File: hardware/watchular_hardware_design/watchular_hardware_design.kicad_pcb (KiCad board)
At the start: 4 copper layers, 55.5 x 22.9 mm, 90 parts, among them J1 USB4105-GF-A, J2 665102131822, J3 TSW-116-07-H-S, J4 TSW-116-07-H-S, Q1 BSS123, Q2 BSS123, Q3 BSS123, Q4 BSS123, T1 DMG1013UW-7, U1 MCP73832T-2DCI/OT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

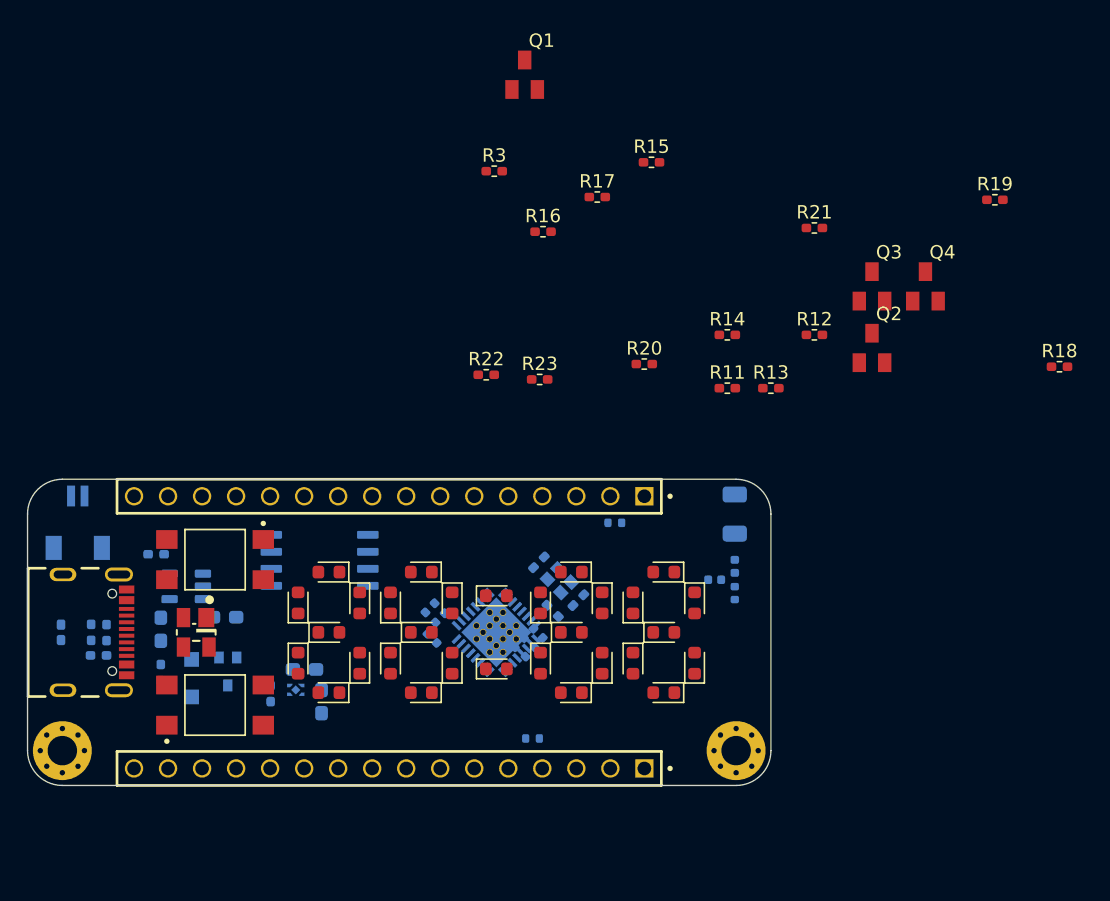
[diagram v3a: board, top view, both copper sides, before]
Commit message: Places LED drivers.
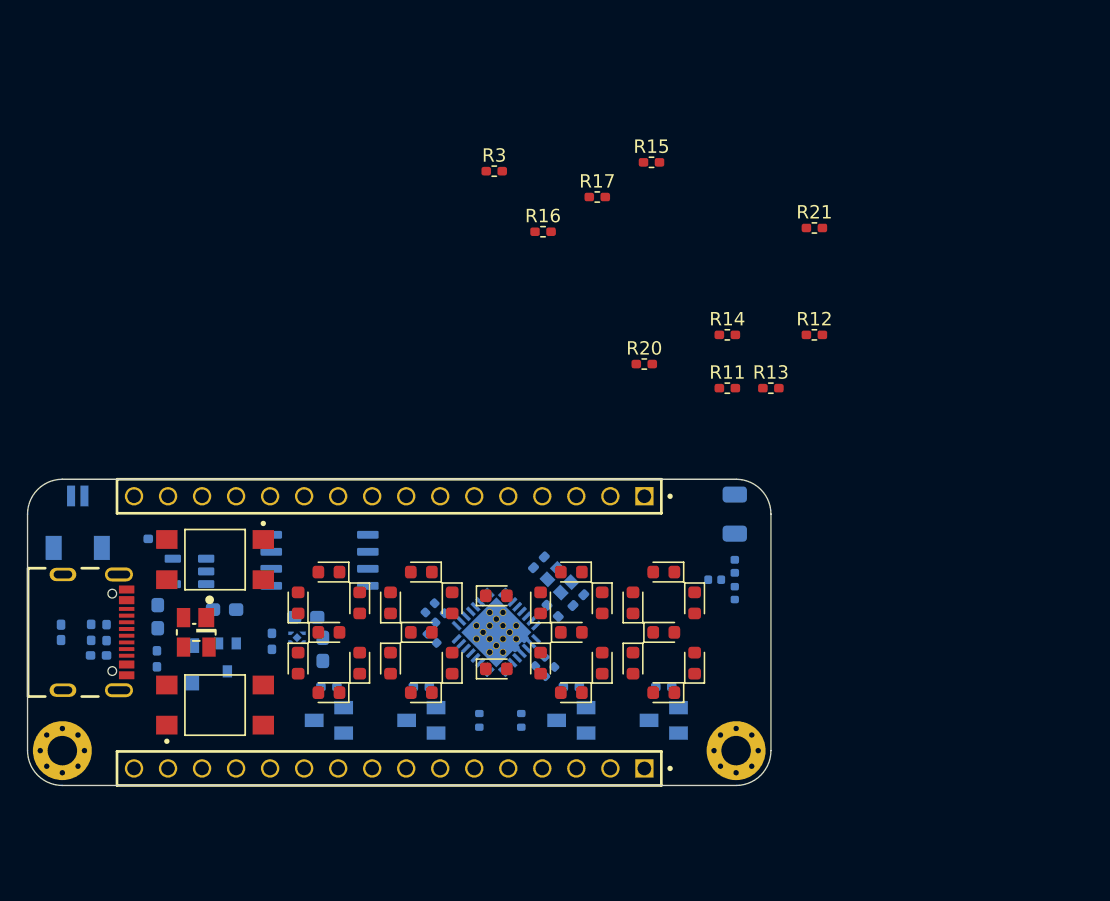
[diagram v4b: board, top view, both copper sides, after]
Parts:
- Q1, Q2, Q3, Q4, R18, R19, R22, R23: moved to B.Cu
- moved R18 59.5 mm to (112.5, 125.5), turned to 180 degrees
- moved R19 56.2 mm to (119.4, 125.5), turned to 180 degrees
- moved Q1 50.4 mm to (112.5, 128.0), turned to -90 degrees
- moved Q2 43.6 mm to (119.4, 128.0), turned to -90 degrees
- moved Q3 39.4 mm to (130.6, 128.0), turned to -90 degrees
- moved Q4 37.8 mm to (137.5, 128.0), turned to -90 degrees
- moved R23 24.7 mm to (137.5, 125.5)
- moved R22 24.2 mm to (130.6, 125.5)
- moved R8 17.9 mm to (123.7, 128.0), turned to 90 degrees
- moved C3 3.90 mm to (110.8, 120.3)
- moved R7 3.90 mm to (108.2, 122.1)
- moved C6 3.90 mm to (112.0, 122.7)
- moved U3 3.90 mm to (110.1, 121.8)
- moved C12 2.10 mm to (128.2, 123.6), turned to -135 degrees
- moved L3 2.07 mm to (129.0, 124.4)
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
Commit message: All the components are on the board.
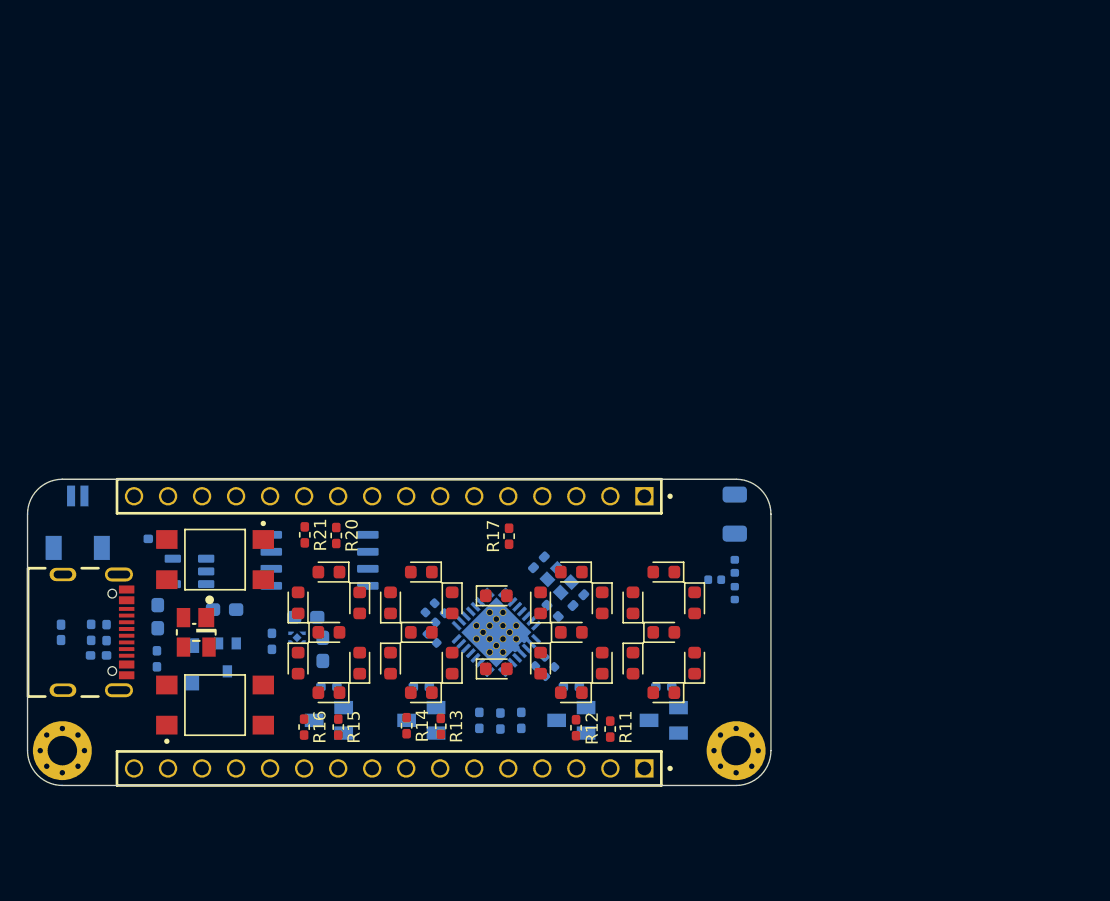
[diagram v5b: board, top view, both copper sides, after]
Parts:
- R3: moved to B.Cu
- R8, R9: footprint Resistor_SMD:R_0402_1005Metric -> Resistor_SMD:R_0402_1005Metric_Pad0.72x0.64mm_HandSolder
- moved R15 48.2 mm to (113.2, 128.5), turned to -90 degrees
- moved R21 44.4 mm to (110.7, 114.2), turned to -90 degrees
- moved R16 41.1 mm to (110.7, 128.5), turned to -90 degrees
- moved R3 41.1 mm to (125.3, 128.1), turned to 90 degrees
- moved R14 37.7 mm to (118.3, 128.4), turned to -90 degrees
- moved R13 35.3 mm to (120.8, 128.4), turned to -90 degrees
- moved R12 34.3 mm to (130.9, 128.6), turned to 90 degrees
- moved R11 26.9 mm to (133.5, 128.7), turned to -90 degrees
- moved R20 26.3 mm to (113.0, 114.2), turned to -90 degrees
- moved R17 26.2 mm to (126.0, 114.2), turned to 90 degrees
- turned R8 to -90 degrees
- turned R9 to -90 degrees

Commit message: Front panel fixed.
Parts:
- moved R21 2.50 mm to (113.2, 114.2)
- moved R20 2.40 mm to (110.7, 114.2)
- moved R11 0.35 mm to (133.5, 128.3)
- moved R12 0.25 mm to (130.9, 128.3), turned to -90 degrees
- moved R14 0.11 mm to (118.2, 128.5)
- moved R17 0.10 mm to (126.0, 114.2)
- moved R13 0.07 mm to (120.8, 128.5)

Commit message: Let the routing begin.
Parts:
- moved R5 2.40 mm to (93.6, 121.5), turned to 90 degrees
- moved C1 2.23 mm to (100.5, 118.2)
- moved U1 2.00 mm to (102.4, 114.9)
- moved C3 2.00 mm to (108.8, 120.3), turned to 180 degrees
- moved C2 1.62 mm to (104.3, 118.2), turned to -90 degrees
- moved R6 0.79 mm to (100.5, 123.5)
- moved R8 0.63 mm to (123.1, 128.0)
- moved R4 0.45 mm to (99.5, 114.9), turned to -90 degrees
- moved D1 0.40 mm to (102.4, 123.5)
- moved C6 0.33 mm to (112.1, 122.4)
- moved R7 0.32 mm to (108.5, 122.2)
- moved R3 0.30 mm to (125.0, 128.0)
- moved T1 0.15 mm to (104.9, 123.5)
- moved D2 0.05 mm to (92.5, 121.5)

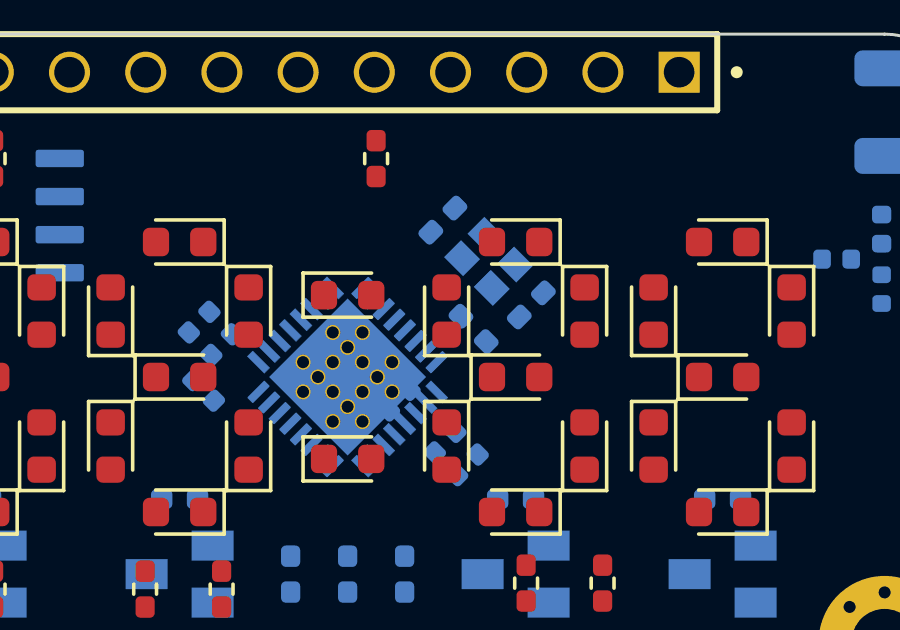
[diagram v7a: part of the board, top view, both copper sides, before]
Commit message: Added 3d for headers. Fixed all the errors.
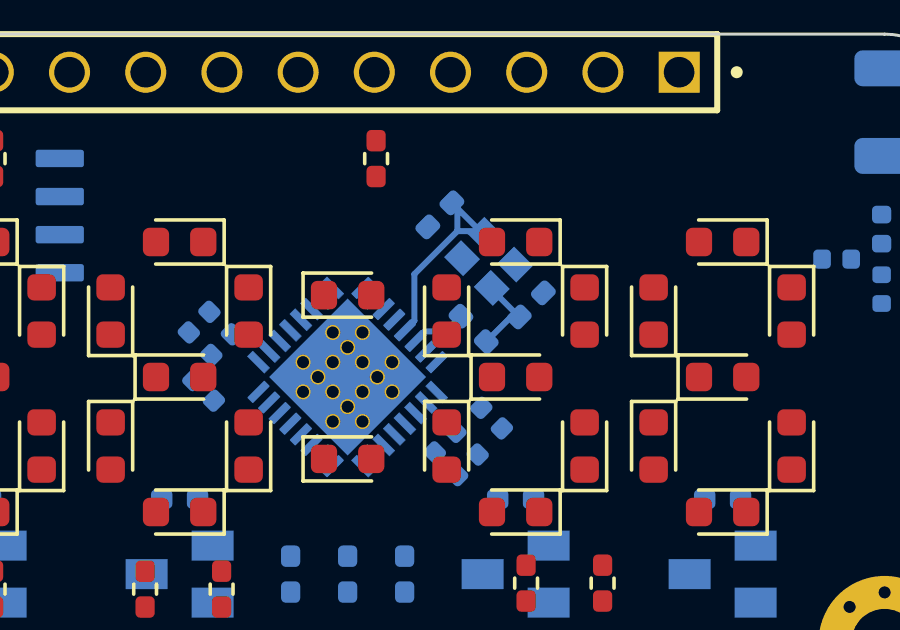
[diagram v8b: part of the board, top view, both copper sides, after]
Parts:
- moved C11 3.14 mm to (129.8, 122.8), turned to -45 degrees
- moved C4 0.20 mm to (128.1, 116.0)
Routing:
- net XTAL_N: track 0.00 -> 7.60 mm
- net Net-(C5-Pad1): track 0.00 -> 2.79 mm
- net XTAL_P: track 0.00 -> 1.86 mm
